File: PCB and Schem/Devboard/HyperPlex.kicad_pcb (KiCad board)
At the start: 2 copper layers, 23.2 x 47.8 mm, 27 parts, among them J1 USB_C_Receptacle_USB2.0_16P, Q1 2N3904, SW1 SW_Push, SW2 SW_SPDT, U1 CH32V203CxTx, U2 TP4056-42-ESOP8, U3 XC6206PxxxMR

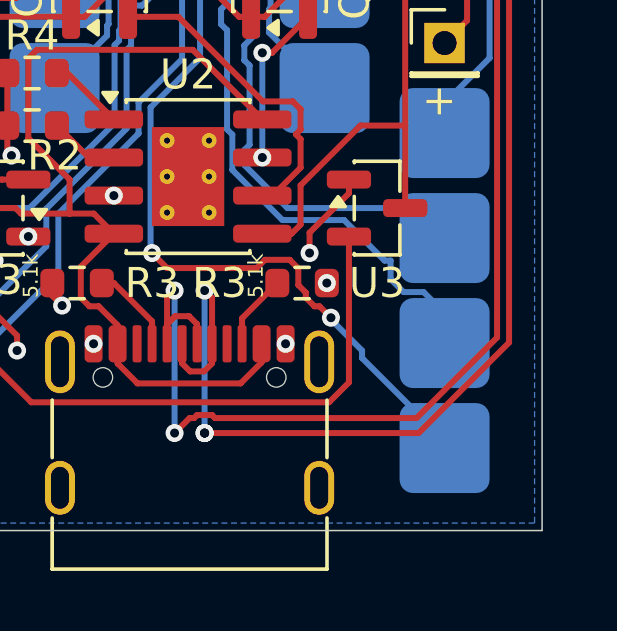
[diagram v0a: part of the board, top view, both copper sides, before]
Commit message: Added Hack Club logo and name to PCB
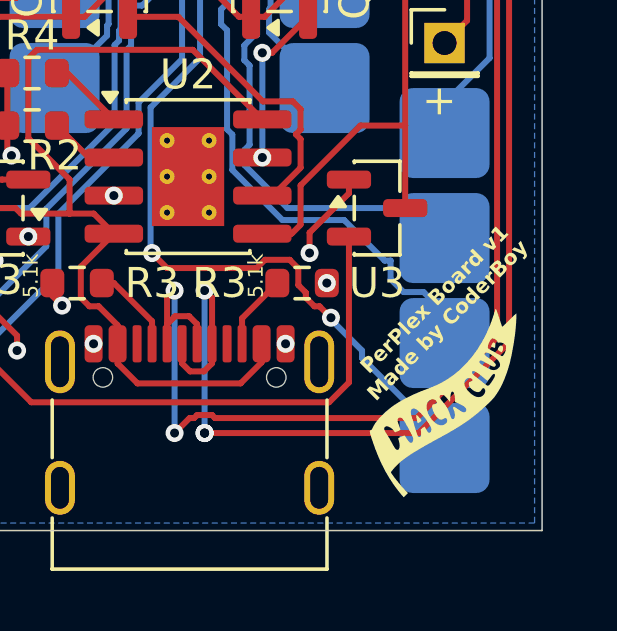
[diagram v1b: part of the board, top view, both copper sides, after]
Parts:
- added G***: LOGO, LOGO, F.Cu at (51.2, 90.5)
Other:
- board text added: "PerPlex Board v1 Made by CoderBoy"

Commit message: Updated journals, added photos
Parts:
- removed HyperPlex: HyperPlex Connector, HyperPlex:HyperPlex Connector
- removed the Q1 at (39.5, 76.9)
- removed the Q1 at (45.5, 76.9)
- removed the R1 at (39.6, 70.5)
- removed the R1 at (45.4, 70.5)
- removed the REF** at (51.0, 78.8)
- removed the REF** at (34.0, 78.8)
- added REF**: BUS_AT, Connector_PCBEdge:BUS_AT, F.Cu at (180.9, 121.3)
- moved R1 149.6 mm to (178.1, 103.5), turned to 180 degrees
- moved R4 143.1 mm to (179.8, 93.0), turned to -90 degrees
- moved R2 142.7 mm to (179.8, 89.2), turned to 90 degrees
- moved R13 141.4 mm to (179.9, 77.5), turned to 0 degrees
- moved R4 137.5 mm to (168.4, 102.2), turned to 180 degrees
- moved SW1 132.8 mm to (174.6, 97.2)
- moved U2 132.0 mm to (174.3, 89.8), turned to 180 degrees
- moved U1 131.7 mm to (161.9, 109.7)
- moved J1 131.6 mm to (172.9, 74.5), turned to 180 degrees
- moved SW1 130.9 mm to (165.9, 97.2)
- moved Q1 129.1 mm to (174.1, 103.0), turned to -90 degrees
- moved G*** 125.9 mm to (175.4, 111.0)
- moved D1 125.7 mm to (167.3, 89.8), turned to -90 degrees
- moved D1 124.3 mm to (165.6, 89.9), turned to 90 degrees
- moved SW2 123.8 mm to (157.9, 74.2), turned to 180 degrees
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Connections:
- D1 pad 1: Net-(D2-K) -> Net-(Q2-B)
- D1 pad 1: Net-(D1-K) -> Net-(Q1-B)
- U2 pad 5: /3.3VRAW -> +3.3V
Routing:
- net +3.3V: track 13.6 -> 99.4 mm, vias 0 -> 4
- net GND: track 95.4 -> 16.4 mm, vias 15 -> 13
- net /3.3V: track 65.5 -> 24.9 mm, vias 2 -> 3
- net Net-(SW3-A): track 42.0 -> 5.58 mm
- net unconnected-(U1-PA2-Pad12): track 40.4 -> 7.00 mm, vias 1 -> 0
- net unconnected-(U1-PA1-Pad11): track 38.0 -> 8.25 mm, vias 1 -> 0
- net unconnected-(U1-PA9-Pad30): track 5.50 -> 33.5 mm
- net unconnected-(U1-PA15-Pad38): track 5.68 -> 32.5 mm
- net unconnected-(U1-PB15-Pad28): track 54.5 -> 30.7 mm, vias 3 -> 1
- net unconnected-(U1-PB14-Pad27): track 6.91 -> 30.1 mm
- net unconnected-(U1-PB12-Pad25): track 5.71 -> 27.8 mm
- net unconnected-(U1-PA8-Pad29): track 50.4 -> 29.1 mm
- net unconnected-(U1-PB7-Pad43): track 6.46 -> 27.1 mm, vias 1 -> 0
- net /USBDP: track 70.7 -> 50.4 mm, vias 3 -> 0
- net /USBDN: track 70.2 -> 50.1 mm, vias 2 -> 0
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- added copper zone on F.Cu, net /3.3V
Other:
- board size 23.2 x 47.8 mm -> 46.2 x 54 mm
- board text added: "3.3vBAT"
- board text added: "G"
- board text added: "LIPO"
- board text added: "OFF"
- board text added: "PerPlex Board v2 Made by CoderBoy"
- board text added: "USB"
- board text added: "V"
- board text removed: "+"
- board text removed: "1.5k"
- board text removed: "10k"
- board text removed: "3.3V"
- board text removed: "5.1k"
- board text removed: "500"
- board text removed: "GND"
- board text removed: "PerPlex Board v1 Made by CoderBoy"
